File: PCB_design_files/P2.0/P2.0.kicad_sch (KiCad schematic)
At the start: 58 parts, among them J1 EEG_IN, J2 20021121-00008C4LF, U1 INA819IDRGR, U2 TLV9102, U3 TPS61094, U4 TPS60400, U5 NRF52832-QFAA-R, Y1 32MHz

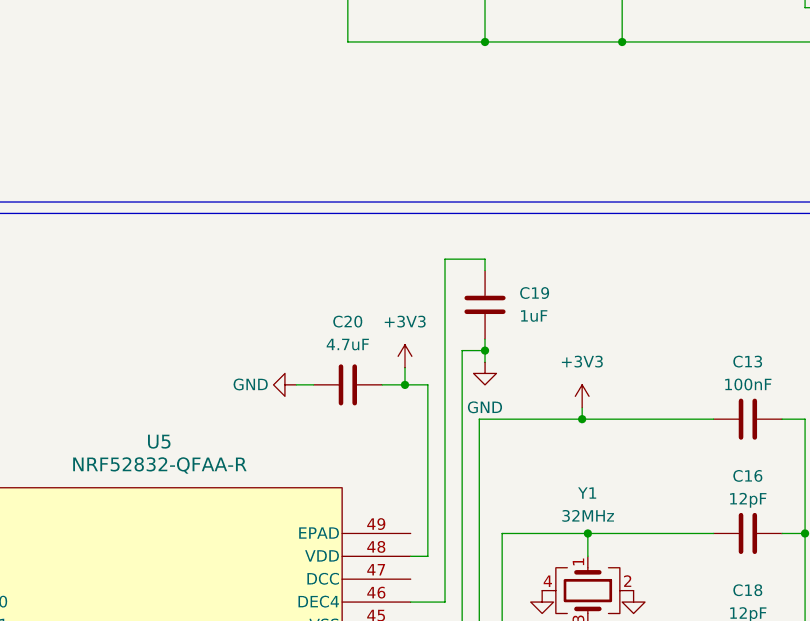
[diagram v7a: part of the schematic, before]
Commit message: Changed C19, C12 footprints
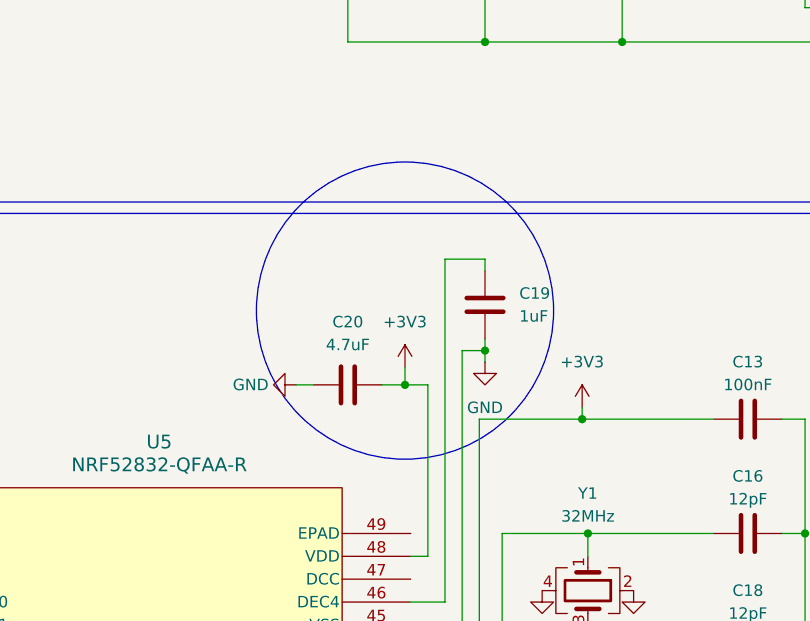
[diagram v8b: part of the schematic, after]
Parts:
- C19, C20: footprint Capacitor_SMD:C_0402_1005Metric -> Capacitor_SMD:C_0603_1608Metric
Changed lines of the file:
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@@
     (stroke (width 0) (type default))
+  )
+  (circle (center 109.22 100.965) (radius 16.51)
+    (stroke (width 0) (type default))
+    (fill (type none))
   )
   (rectangle (start 162.56 90.17) (end 340.36 167.64)
@@
       (effects (font (size 1.27 1.27)) (justify left))
     )
-    (property "Footprint" "Capacitor_SMD:C_0402_1005Metric" (at 119.0752 104.14 0)
-      (effects (font (size 1.27 1.27)) hide)
-    )
-    (property "Datasheet" "https://search.murata.co.jp/Ceramy/image/img/A01X/G101/ENG/GRM155R70J105KA12-01.pdf" (at 118.11 100.33 0)
+    (property "Footprint" "Capacitor_SMD:C_0603_1608Metric" (at 119.0752 104.14 0)
+      (effects (font (size 1.27 1.27)) hide)
+    )
+    (property "Datasheet" "" (at 118.11 100.33 0)
       (effects (font (size 1.27 1.27)) hide)
     )
@@
       (effects (font (size 1.27 1.27)))
     )
-    (property "Footprint" "Capacitor_SMD:C_0402_1005Metric" (at 99.06 110.1852 0)
-      (effects (font (size 1.27 1.27)) hide)
-    )
-    (property "Datasheet" "https://search.murata.co.jp/Ceramy/image/img/A01X/G101/ENG/GRM155R60J475ME47-01.pdf" (at 102.87 109.22 0)
-      (effects (font (size 1.27 1.27)) hide)
-    )
+    (property "Footprint" "Capacitor_SMD:C_0603_1608Metric" (at 99.06 110.1852 0)
+      (effects (font (size 1.27 1.27)) hide)
+    )
+    (property "Datasheet" "" (at 102.87 109.22 0)
+      (effects (font (size 1.27 1.27)) hide)
+    )
